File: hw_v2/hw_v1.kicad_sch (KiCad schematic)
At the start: 55 parts, among them J16 47352-1001, J8 USB_B, J9 Tag connect, SW2 SW_Push, U13 STM32F407VGTx, U14 TJA1051T-3, U15 25Q16, U16 REF3033, U17 SRV05-4, Y1 32.768kHz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

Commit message: wip v7
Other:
- removed sheet Protoboard
- sheet Sensors ports: added none; removed ext_a0_in, ext_a1_in
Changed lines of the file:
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@@
 	)
 	(bus_entry
-		(at 199.39 116.84)
-		(size 2.54 -2.54)
-		(stroke
-			(width 0)
-			(type default)
-		)
-	)
-	(bus_entry
 		(at 278.13 91.44)
 		(size 2.54 -2.54)
@@
 	)
 	(bus_entry
-		(at 201.93 105.41)
-		(size 2.54 2.54)
-		(stroke
-			(width 0)
-			(type default)
-		)
-	)
-	(bus_entry
 		(at 201.93 87.63)
 		(size 2.54 2.54)
@@
 	)
 	(bus_entry
-		(at 201.93 102.87)
-		(size 2.54 2.54)
-		(stroke
-			(width 0)
-			(type default)
-		)
-	)
-	(bus_entry
 		(at 88.9 66.04)
 		(size 2.54 2.54)
@@
 	)
 	(bus_entry
-		(at 199.39 114.3)
-		(size 2.54 -2.54)
-		(stroke
-			(width 0)
-			(type default)
-		)
-	)
-	(bus_entry
 		(at 276.86 154.94)
 		(size 2.54 -2.54)
@@
 	(wire
 		(pts
-			(xy 204.47 105.41) (xy 205.74 105.41)
-		)
-		(stroke
-			(width 0)
-			(type default)
-		)
-	)
-	(wire
-		(pts
 			(xy 81.28 124.46) (xy 95.25 124.46)
 		)
@@
 		)
 	)
-	(bus
-		(pts
-			(xy 201.93 102.87) (xy 201.93 105.41)
-		)
-		(stroke
-			(width 0)
-			(type default)
-		)
-	)
 	(wire
 		(pts
@@
 	(wire
 		(pts
-			(xy 198.12 116.84) (xy 199.39 116.84)
-		)
-		(stroke
-			(width 0)
-			(type default)
-		)
-	)
-	(wire
-		(pts
 			(xy 161.29 139.7) (xy 154.94 139.7)
 		)
@@
 		)
 	)
-	(wire
-		(pts
-			(xy 204.47 107.95) (xy 205.74 107.95)
-		)
-		(stroke
-			(width 0)
-			(type default)
-		)
-	)
 	(bus
 		(pts
@@
 	(wire
 		(pts
-			(xy 198.12 114.3) (xy 199.39 114.3)
-		)
-		(stroke
-			(width 0)
-			(type default)
-		)
-	)
-	(wire
-		(pts
 			(xy 55.88 38.1) (xy 55.88 40.64)
 		)
@@
 		)
 	)
-	(bus
-		(pts
-			(xy 201.93 111.76) (xy 201.93 114.3)
-		)
-		(stroke
-			(width 0)
-			(type default)
-		)
-	)
 	(wire
 		(pts
@@
 		)
 	)
-	(bus
-		(pts
-			(xy 201.93 105.41) (xy 201.93 111.76)
-		)
-		(stroke
-			(width 0)
-			(type default)
-		)
-	)
 	(wire
 		(pts
@@
 	)
 	(label "SPI2_MOSI"
-		(at 177.8 124.46 180)
-		(fields_autoplaced yes)
-		(effects
-			(font
-				(size 0.7874 0.7874)
-			)
-			(justify right bottom)
-		)
-	)
-	(label "SPI2_MOSI"
 		(at 83.82 129.54 0)
 		(fields_autoplaced yes)
@@
 		)
 	)
-	(label "SPI2_MISO"
-		(at 177.8 121.92 180)
-		(fields_autoplaced yes)
-		(effects
-			(font
-				(size 0.7874 0.7874)
-			)
-			(justify right bottom)
-		)
-	)
 	(label "CEL_OUT"
 		(at 83.82 134.62 0)
@@
 		)
 	)
-	(label "SPI2_SCK"
-		(at 177.8 127 180)
-		(fields_autoplaced yes)
-		(effects
-			(font
-				(size 0.7874 0.7874)
-			)
-			(justify right bottom)
-		)
-	)
 	(label "LED2"
 		(at 182.88 97.79 180)
@@
 	)
 	(sheet
-		(at 177.8 110.49)
-		(size 20.32 17.78)
-		(stroke
-			(width 0.1524)
-			(type solid)
-		)
-		(fill
-			(color 0 0 0 0.0000)
-		)
-		(property "Sheetname" "Protoboard"
-			(at 177.8 109.7784 0)
-			(effects
-				(font
-					(size 1.27 1.27)
-				)
-				(justify left bottom)
-			)
-		)
-		(property "Sheetfile" "protoboard.kicad_sch"
-			(at 177.546 129.032 0)
-			(effects
-				(font
-					(size 1 1)
-				)
-				(justify left top)
-			)
-		)
-		(pin "ext_a0_in" input
-			(at 198.12 114.3 0)
-			(effects
-				(font
-					(size 1.27 1.27)
-				)
-				(justify right)
-			)
-		)
-		(pin "ext_a1_in" input
-			(at 198.12 116.84 0)
-			(effects
-				(font
-					(size 1.27 1.27)
-				)
-				(justify right)
-			)
-		)
-		(pin "SPI2_MISO" input
-			(at 177.8 121.92 180)
-			(effects
-				(font
-					(size 1.27 1.27)
-				)
-				(justify left)
-			)
-		)
-		(pin "SPI2_MOSI" input
-			(at 177.8 124.46 180)
-			(effects
-				(font
-					(size 1.27 1.27)
-				)
-				(justify left)
-			)
-		)
-		(pin "SPI2_SCK" input
-			(at 177.8 127 180)
-			(effects
-				(font
-					(size 1.27 1.27)
-				)
-				(justify left)
-			)
-		)
-		(instances
-			(project "hw_v1"
-				(path "/b3feb07e-be80-40e1-bd13-6cd54c2f8b0c"
-					(page "7")
-				)
-			)
-		)
-	)
-	(sheet
 		(at 246.38 119.38)
 		(size 27.94 15.24)
@@
 			)
 		)
-		(pin "ext_a0_in" input
-			(at 205.74 107.95 180)
-			(effects
-				(font
-					(size 1.27 1.27)
-				)
-				(justify left)
-			)
-		)
 		(pin "ext_a1_out" input
 			(at 233.68 88.9 0)
@@
 			)
 		)
-		(pin "ext_a1_in" input
-			(at 205.74 105.41 180)
-			(effects
-				(font
-					(size 1.27 1.27)
-				)
-				(justify left)
-			)
-		)

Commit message: hw v2
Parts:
- added C6: 100nF, Capacitor_SMD:C_0805_2012Metric, symbol Device:C_Small
- added SW1: SW_Push, Button_Switch_SMD:SW_SPST_CK_RS282G05A3, symbol Switch:SW_Push
- SW2: footprint Button_Switch_SMD:SW_SPST_TL3342 -> Button_Switch_SMD:SW_SPST_CK_RS282G05A3
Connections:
- net +3V3: now also SW1.2
- net EXT_0: no longer U13.31 (PA6)
- net EXT_1: no longer U13.32 (PA7)
- net GND: now also C6.1
- net PMIC1_CS: no longer U13.48 (PB11)
- net PMIC1_ENABLE: no longer U13.51 (PB12)
- net at R27.1, TP7.1, U13.94 (BOOT0): now also C6.2, SW1.1
- net MCU-D0: no longer names the net of U13.35 (PB0)
- net MCU-D1: no longer names the net of U13.36 (PB1)
- no-connect marks 10 -> 16
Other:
- moved on the sheet: R27, SW2

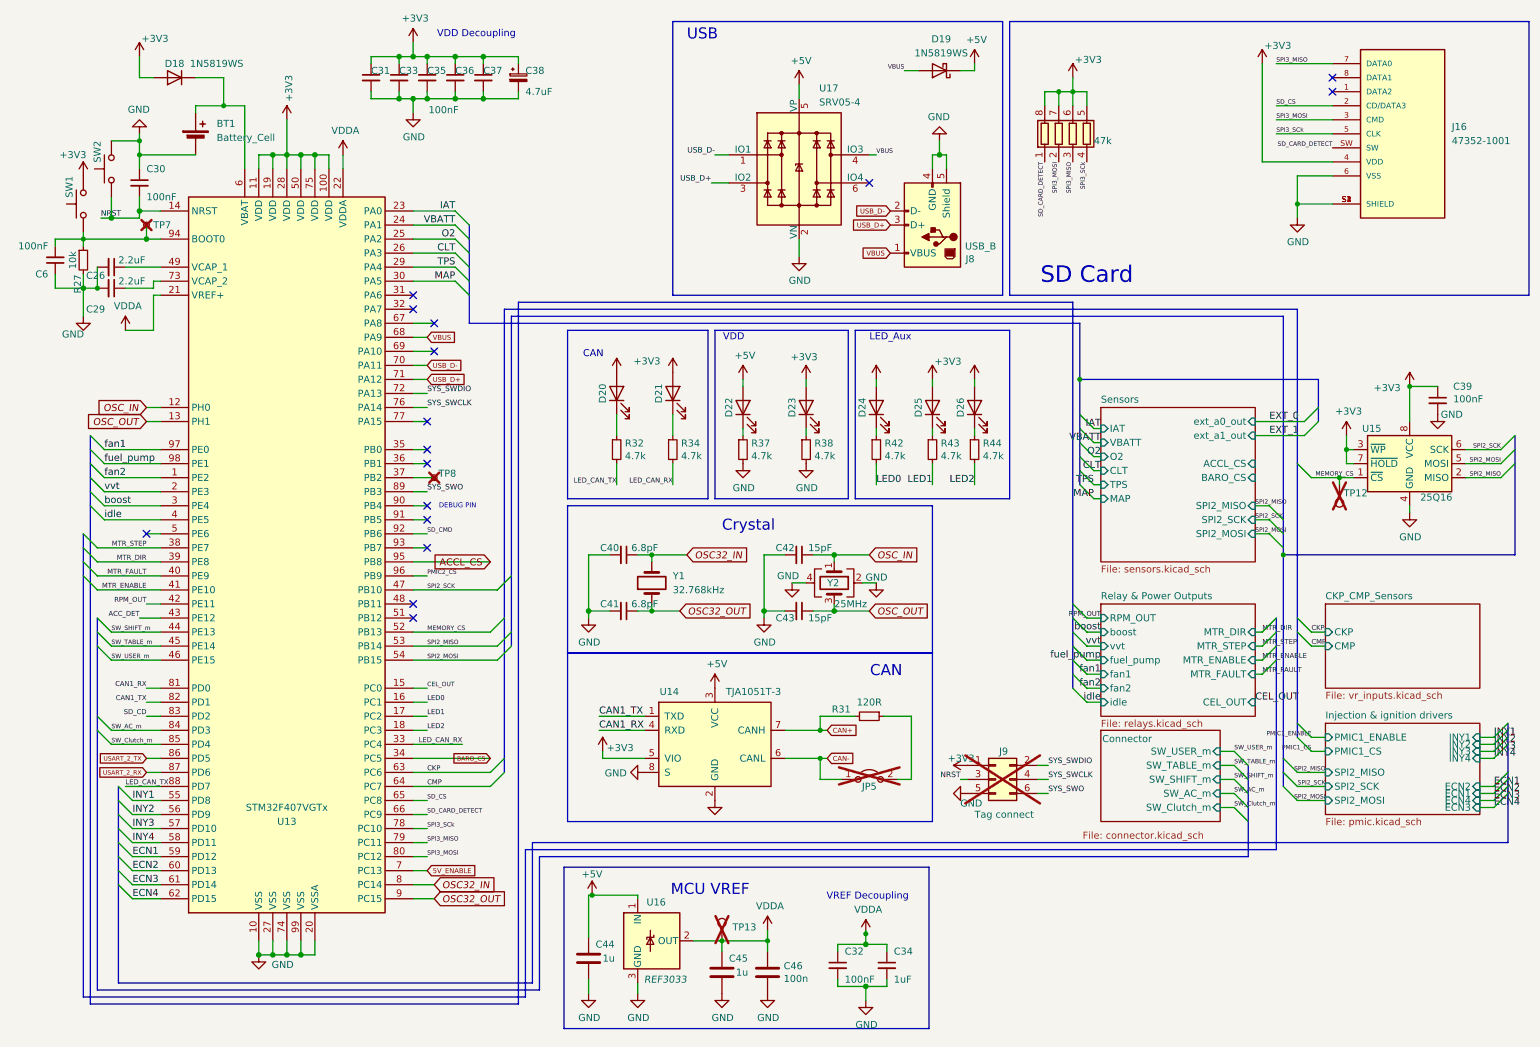
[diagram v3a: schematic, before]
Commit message: fix LCSC codes
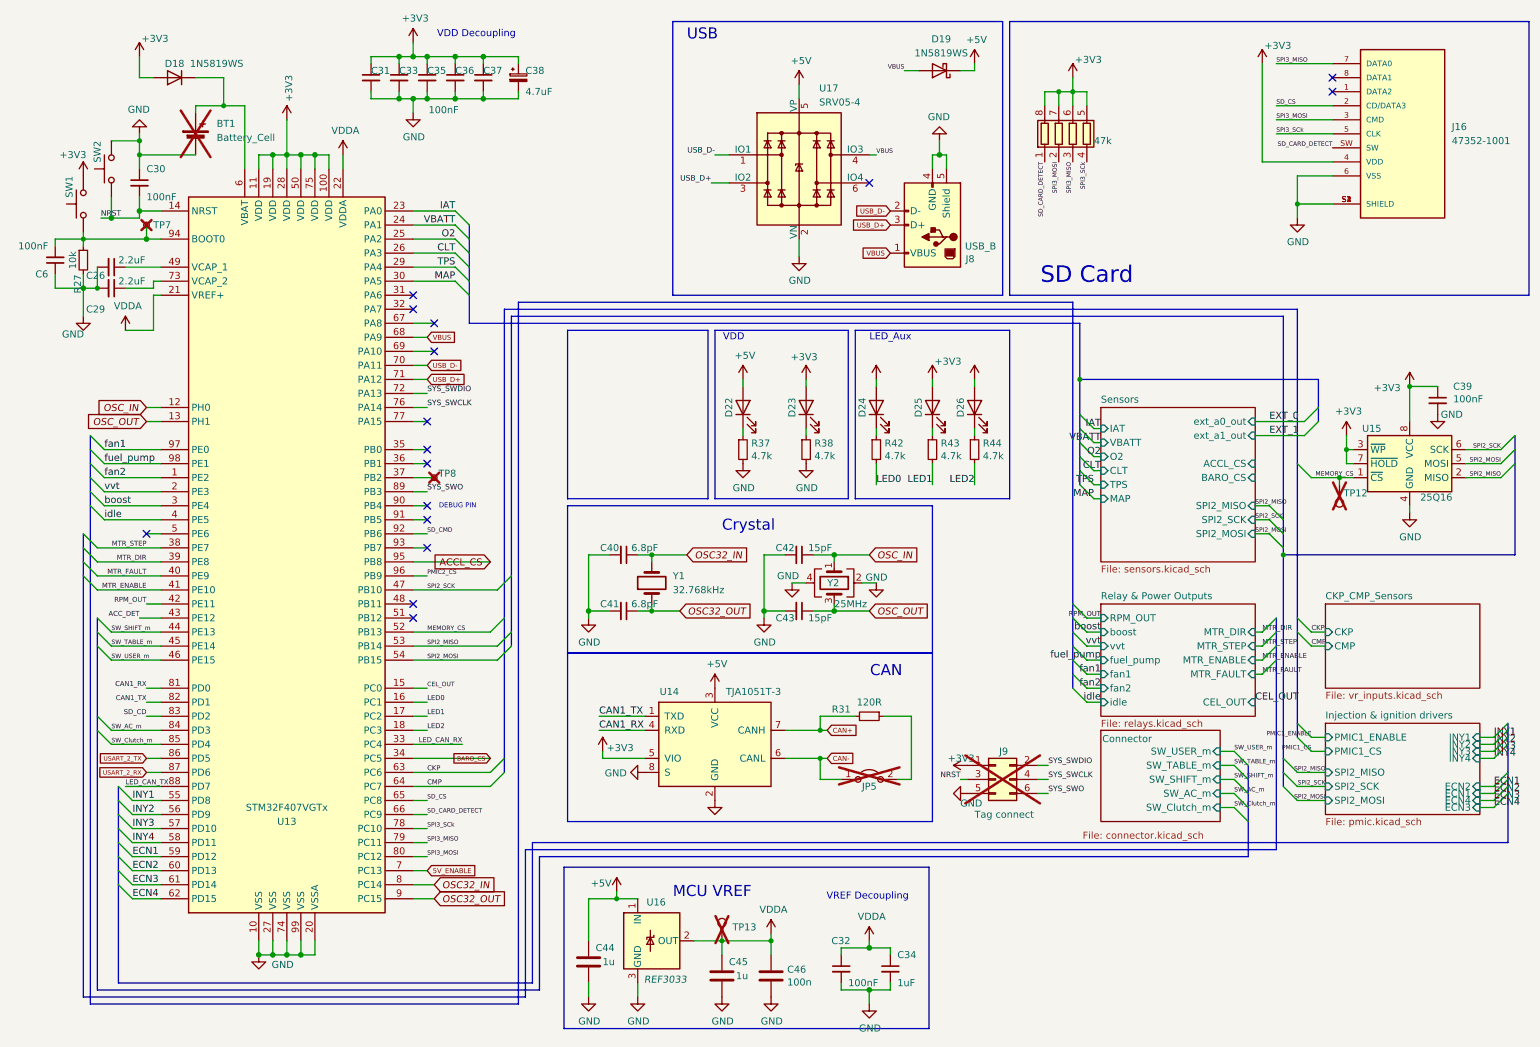
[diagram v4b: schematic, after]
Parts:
- removed D20, D21: LED, LED_SMD:LED_0805_2012Metric, symbol Device:LED
- removed R32, R34: 4.7k, Resistor_SMD:R_0603_1608Metric, symbol Device:R_Small
- BT1: now not fitted
- C46: LCSC C38141 -> C49678
- SW1, SW2: now in the parts list
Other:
- moved on the sheet: C32, C34, C44, C45, C46

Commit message: wip analog frontend & power
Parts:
- added R10: 10k, Resistor_SMD:R_0603_1608Metric, symbol Device:R_Small
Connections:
- net GND: now also R10.2
- net at TP8.1, U13.37 (PB2): now also R10.1
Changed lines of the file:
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@@
 	)
 	(junction
+		(at 85.09 96.52)
+		(diameter 0)
+		(color 0 0 0 0)
+	)
+	(junction
 		(at 163.83 189.23)
 		(diameter 1.016)
@@
 	(wire
 		(pts
+			(xy 105.41 105.41) (xy 105.41 109.22)
+		)
+		(stroke
+			(width 0)
+			(type default)
+		)
+	)
+	(wire
+		(pts
 			(xy 135.255 43.18) (xy 138.43 43.18)
 		)
@@
 	(wire
 		(pts
+			(xy 85.09 96.52) (xy 105.41 96.52)
+		)
+		(stroke
+			(width 0)
+			(type solid)
+		)
+	)
+	(wire
+		(pts
 			(xy 204.47 87.63) (xy 205.74 87.63)
 		)
@@
 	(wire
 		(pts
-			(xy 85.09 96.52) (xy 81.28 96.52)
+			(xy 81.28 96.52) (xy 85.09 96.52)
 		)
 		(stroke
@@
 	(wire
 		(pts
+			(xy 105.41 100.33) (xy 105.41 96.52)
+		)
+		(stroke
+			(width 0)
+			(type default)
+		)
+	)
+	(wire
+		(pts
 			(xy 144.78 121.92) (xy 144.78 120.65)
 		)
@@
 	(symbol
 		(lib_id "power:GND")
+		(at 105.41 109.22 0)
+		(unit 1)
+		(exclude_from_sim no)
+		(in_bom yes)
+		(on_board yes)
+		(dnp no)
+		(property "Reference" "#PWR053"
+			(at 105.41 115.57 0)
+			(effects
+				(font
+					(size 1.27 1.27)
+				)
+				(hide yes)
+			)
+		)
+		(property "Value" "GND"
+			(at 105.537 112.4712 0)
+			(effects
+				(font
+					(size 1.27 1.27)
+				)
+				(justify right)
+			)
+		)
+		(property "Footprint" ""
+			(at 105.41 109.22 0)
+			(effects
+				(font
+					(size 1.27 1.27)
+				)
+				(hide yes)
+			)
+		)
+		(property "Datasheet" ""
+			(at 105.41 109.22 0)
+			(effects
+				(font
+					(size 1.27 1.27)
+				)
+				(hide yes)
+			)
+		)
+		(property "Description" ""
+			(at 105.41 109.22 0)
+			(effects
+				(font
+					(size 1.27 1.27)
+				)
+				(hide yes)
+			)
+		)
+		(pin "1"
+		)
+		(instances
+			(project "hw_v1"
+				(path "/b3feb07e-be80-40e1-bd13-6cd54c2f8b0c"
+					(reference "#PWR053")
+					(unit 1)
+				)
+			)
+		)
+	)
+	(symbol
+		(lib_id "power:GND")
 		(at 135.89 154.94 0)
 		(unit 1)
@@
 					(unit 1)
 				)
+			)
+		)
+	)
+	(symbol
+		(lib_id "Device:R_Small")
+		(at 105.41 102.87 0)
+		(unit 1)
+		(exclude_from_sim no)
+		(in_bom yes)
+		(on_board yes)
+		(dnp no)
+		(property "Reference" "R10"
+			(at 104.394 107.188 90)
+			(effects
+				(font
+					(size 1.27 1.27)
+				)
+			)
+		)
+		(property "Value" "10k"
+			(at 103.505 102.87 90)
+			(effects
+				(font
+					(size 1.27 1.27)
+				)
+			)
+		)
+		(property "Footprint" "Resistor_SMD:R_0603_1608Metric"
+			(at 105.41 102.87 0)
+			(effects
+				(font
+					(size 1.27 1.27)
+				)
+				(hide yes)
+			)
+		)
+		(property "Datasheet" "~"
+			(at 105.41 102.87 0)
+			(effects
+				(font
+					(size 1.27 1.27)
+				)
+				(hide yes)
+			)
+		)
+		(property "Description" ""
+			(at 105.41 102.87 0)
+			(effects
+				(font
+					(size 1.27 1.27)
+				)
+				(hide yes)
+			)
+		)
+		(property "LCSC" "C115324"
+			(at 105.41 102.87 0)
+			(effects
+				(font
+					(size 1.27 1.27)
+				)
+				(hide yes)
+			)
+		)
+		(property "STOCK" "RES-000118-00"
+			(at 105.41 102.87 0)
+			(effects
+				(font
+					(size 1.27 1.27)
+				)
+				(hide yes)
+			)
+		)
+		(pin "1"
+		)
+		(pin "2"
+		)
+		(instances
+			(project "hw_v1"
+				(path "/b3feb07e-be80-40e1-bd13-6cd54c2f8b0c"
+					(reference "R10")
+					(unit 1)
+				)

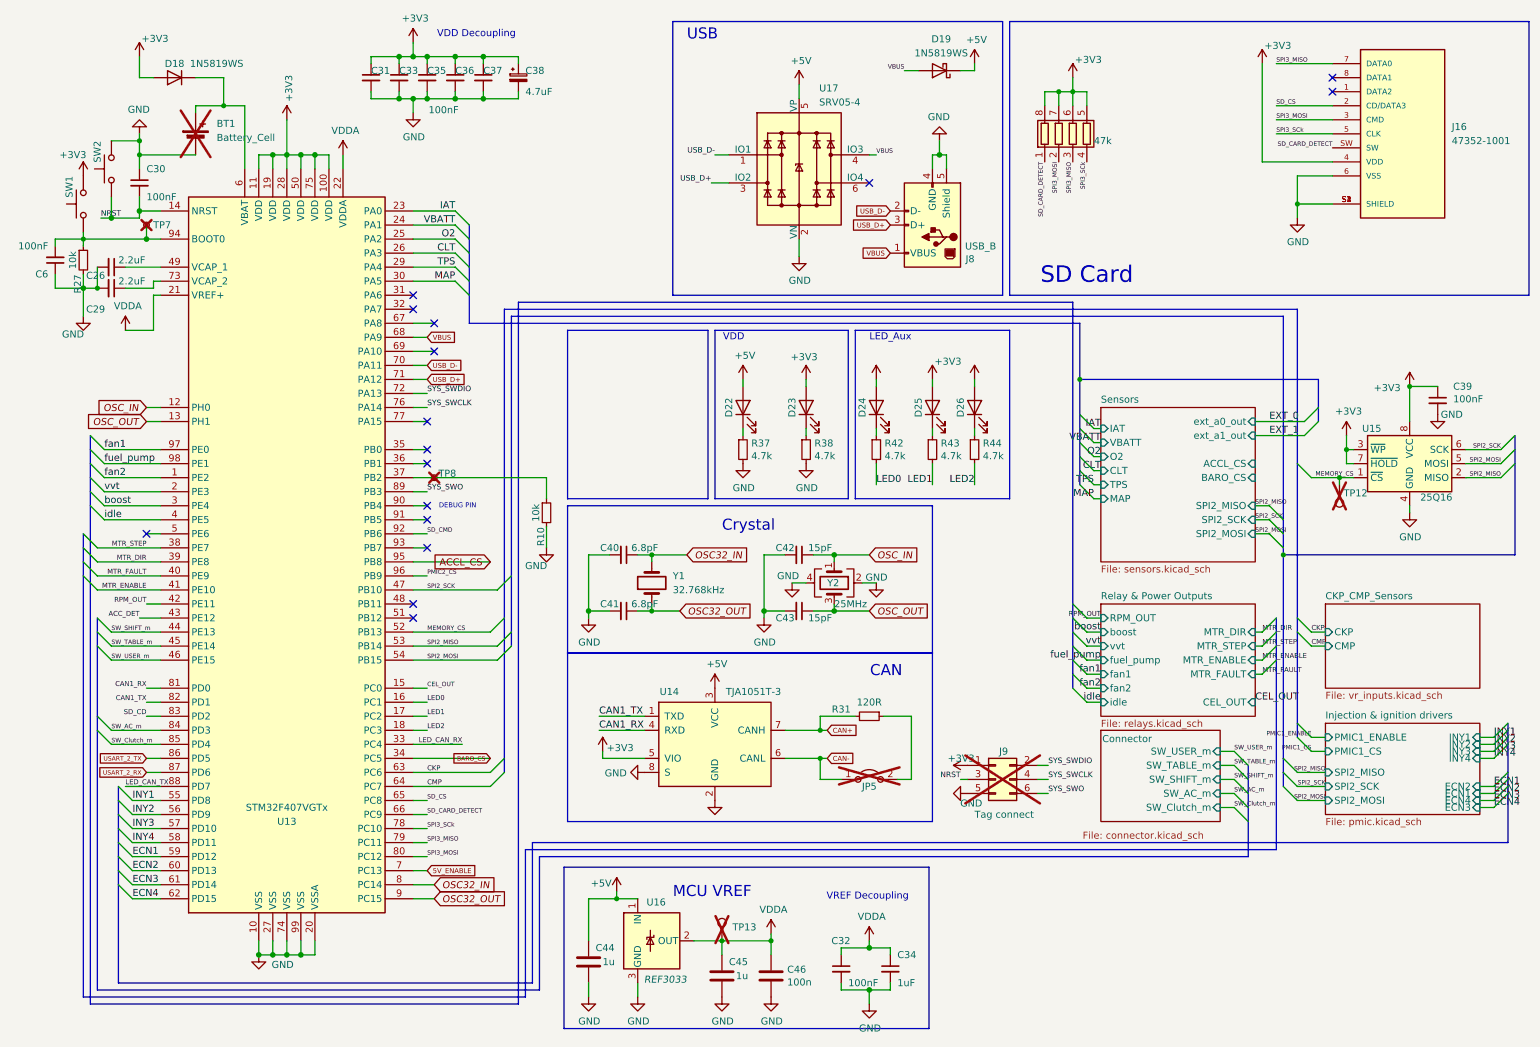
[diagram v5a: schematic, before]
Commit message: Fix some ERC errors
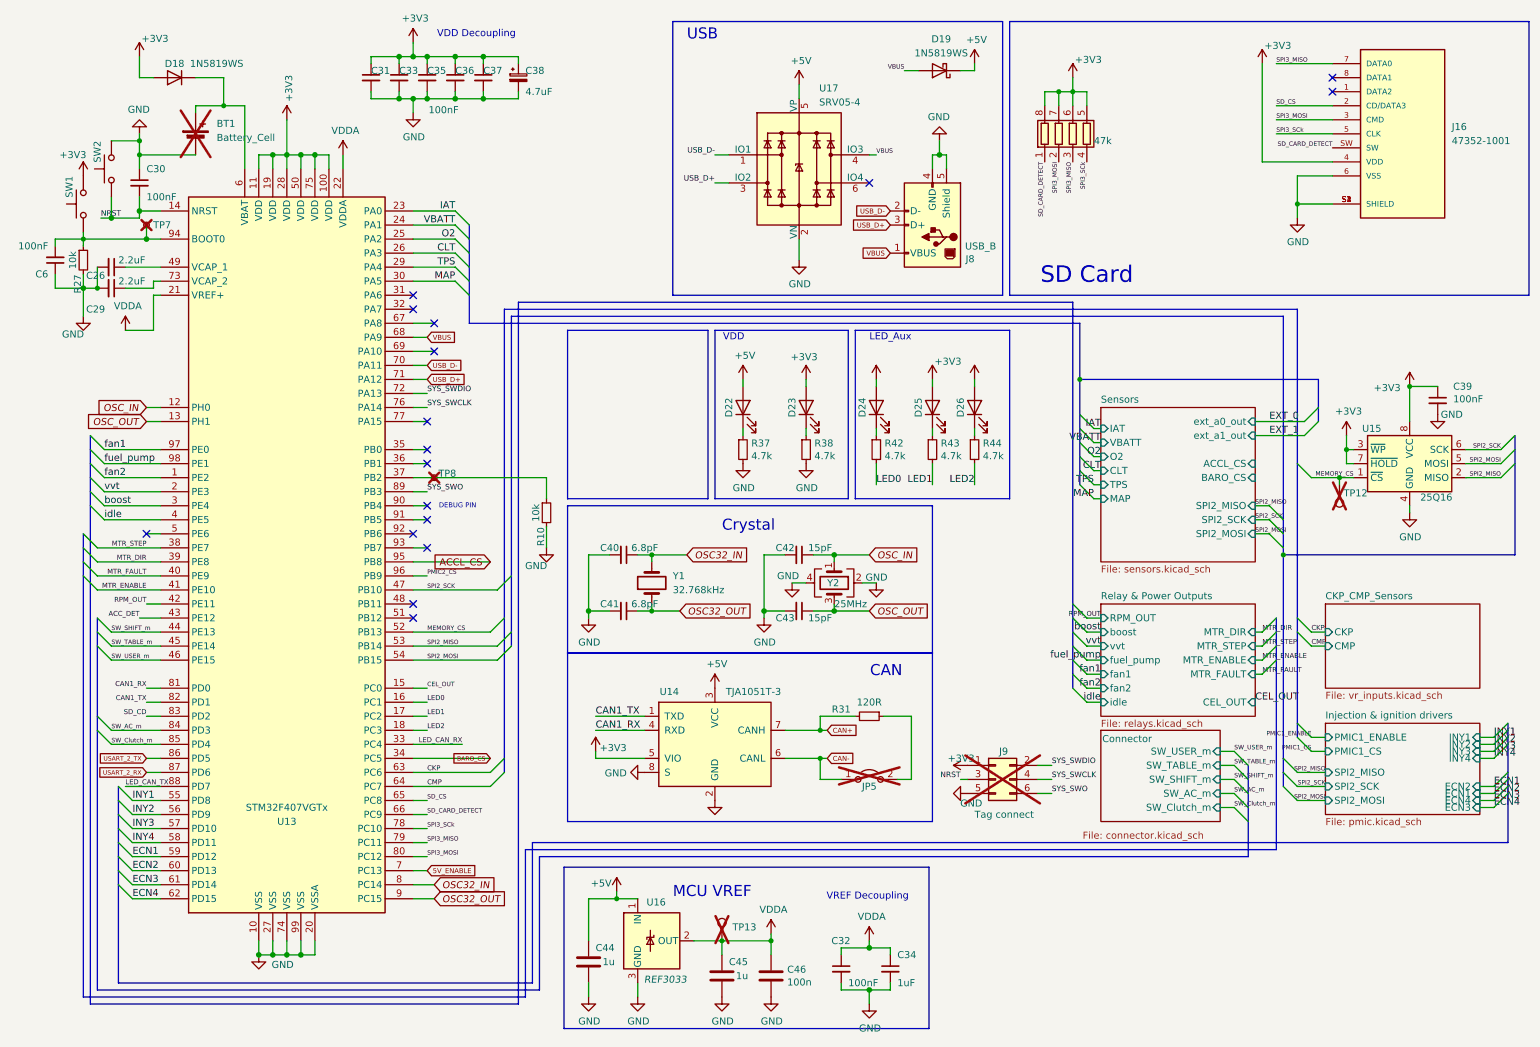
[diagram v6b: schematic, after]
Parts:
- C38: symbol Device:CP_Small -> Device:C_Polarized_Small
- SW1, SW2: LCSC C412370 -> C2888955; STOCK MEC-000125-00 -> (none)
- U14: footprint Package_SO:SOP-8_3.9x4.9mm_P1.27mm -> Package_SO:SOIC-8_3.9x4.9mm_P1.27mm
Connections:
- net SD_CMD: no longer names the net of U13.92 (PB6)
- no-connect marks 16 -> 17
